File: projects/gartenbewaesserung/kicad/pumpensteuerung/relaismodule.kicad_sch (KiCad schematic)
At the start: 5 parts, among them J1 Screw_Terminal_01x03, K2 SANYOU_SRD_Form_C, Q1 S8050

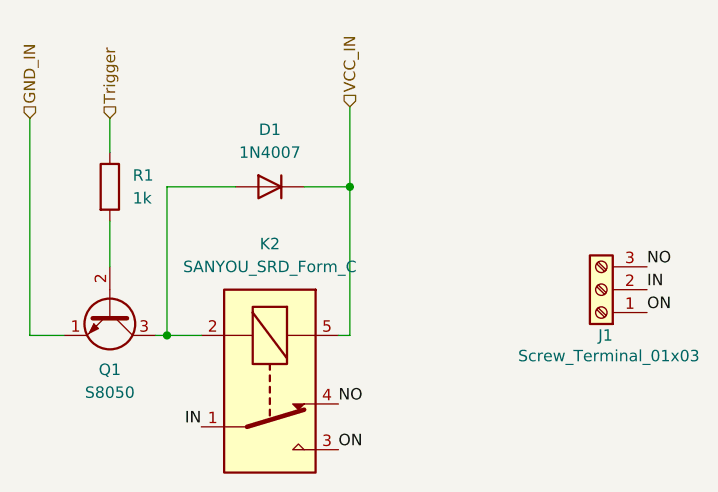
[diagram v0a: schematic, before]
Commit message: [gartenbewaesserung(pcb)] change resistor to 220 Ohm
1k was a little bit too much, for 3.3V.
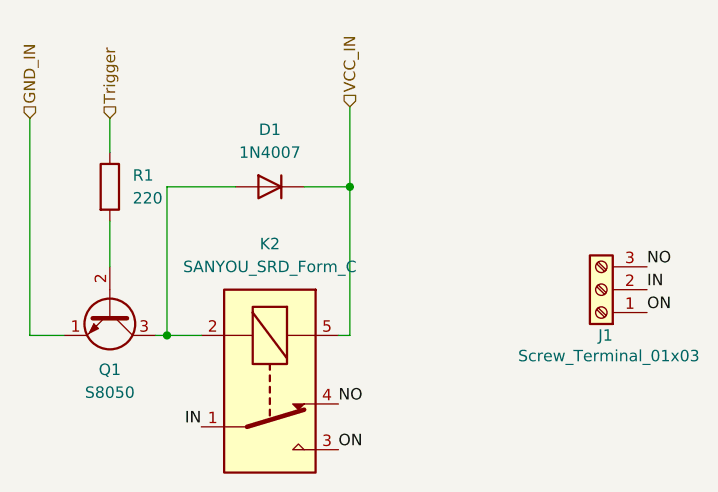
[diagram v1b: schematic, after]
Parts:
- R1: value 1k -> 220; footprint Resistor_THT:R_Axial_DIN0204_L3.6mm_D1.6mm_P7.62mm_Horizontal -> Resistor_THT:R_Axial_DIN0207_L6.3mm_D2.5mm_P7.62mm_Horizontal
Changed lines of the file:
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@@
 			)
 		)
-		(property "Value" "1k"
+		(property "Value" "220"
 			(at 30.48 31.7499 0)
 			(effects
@@
 			)
 		)
-		(property "Footprint" "Resistor_THT:R_Axial_DIN0204_L3.6mm_D1.6mm_P7.62mm_Horizontal"
+		(property "Footprint" "Resistor_THT:R_Axial_DIN0207_L6.3mm_D2.5mm_P7.62mm_Horizontal"
 			(at 26.162 30.48 90)
 			(effects

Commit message: [gartenbewasserung(pcb)] replace Q8050 with a 2N3904
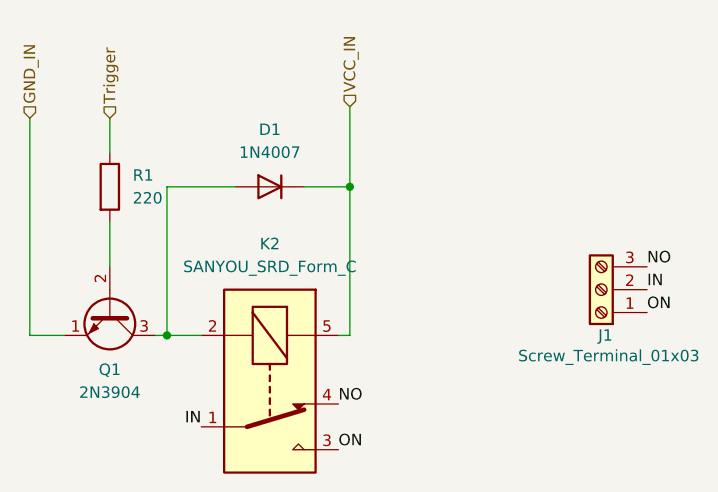
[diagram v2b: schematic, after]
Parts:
- removed Q1: S8050, Package_TO_SOT_THT:TO-92_Inline, symbol Transistor_BJT:S8050
- added Q1: 2N3904, Package_TO_SOT_THT:TO-92_Inline, symbol Transistor_BJT:2N3904
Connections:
- net GND_IN: now also Q1.1 (E)
- net at R1.2: now also Q1.2 (B)
- net at D1.2 (A), K2.2: now also Q1.3 (C)
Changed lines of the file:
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@@
-	)
-	(symbol
-		(lib_id "Transistor_BJT:S8050")
-		(at 27.94 44.45 270)
-		(unit 1)
-		(exclude_from_sim no)
-		(in_bom yes)
-		(on_board yes)
-		(dnp no)
-		(fields_autoplaced yes)
-		(property "Reference" "Q1"
-			(at 27.94 50.8 90)
-			(effects
-				(font
-					(size 1.27 1.27)
-				)
-			)
-		)
-		(property "Value" "S8050"
-			(at 27.94 53.34 90)
-			(effects
-				(font
-					(size 1.27 1.27)
-				)
-			)
-		)
-		(property "Footprint" "Package_TO_SOT_THT:TO-92_Inline"
-			(at 26.035 49.53 0)
-			(effects
-				(font
-					(size 1.27 1.27)
-					(italic yes)
-				)
-				(justify left)
-				(hide yes)
-			)
-		)
-		(property "Datasheet" "http://www.unisonic.com.tw/datasheet/S8050.pdf"
-			(at 27.94 44.45 0)
-			(effects
-				(font
-					(size 1.27 1.27)
-				)
-				(justify left)
-				(hide yes)
-			)
-		)
-		(property "Description" "0.7A Ic, 20V Vce, Low Voltage High Current NPN Transistor, TO-92"
-			(at 27.94 44.45 0)
-			(effects
-				(font
-					(size 1.27 1.27)
-				)
-				(hide yes)
-			)
-		)
-		(pin "3"
-		)
-		(pin "1"
-		)
-		(pin "2"
-		)
-		(instances
-			(project "gartenbewaesserung"
-				(path "/21a07dfa-371b-4773-840e-44a8dfeac208/016a9bfd-fffd-4284-b312-eaf12770d68d"
-					(reference "Q1")
-					(unit 1)
-				)
-				(path "/21a07dfa-371b-4773-840e-44a8dfeac208/63189825-b5eb-44b8-a12d-37b83fa5c151"
-					(reference "Q3")
-					(unit 1)
-				)
-				(path "/21a07dfa-371b-4773-840e-44a8dfeac208/d92ddb11-359c-4ecb-a782-88a2addaf04a"
-					(reference "Q2")
-					(unit 1)
-				)
-			)
-		)
 	)
 	(symbol
@@
 					(unit 1)
 				)
+			)
+		)
+	)
+	(symbol
+		(lib_id "Transistor_BJT:2N3904")
+		(at 27.94 44.45 270)
+		(unit 1)
+		(exclude_from_sim no)
+		(in_bom yes)
+		(on_board yes)
+		(dnp no)
+		(fields_autoplaced yes)
+		(property "Reference" "Q1"
+			(at 27.94 50.8 90)
+			(effects
+				(font
+					(size 1.27 1.27)
+				)
+			)
+		)
+		(property "Value" "2N3904"
+			(at 27.94 53.34 90)
+			(effects
+				(font
+					(size 1.27 1.27)
+				)
+			)
+		)
+		(property "Footprint" "Package_TO_SOT_THT:TO-92_Inline"
+			(at 26.035 49.53 0)
+			(effects
+				(font
+					(size 1.27 1.27)
+					(italic yes)
+				)
+				(justify left)
+				(hide yes)
+			)
+		)
+		(property "Datasheet" "https://www.onsemi.com/pub/Collateral/2N3903-D.PDF"
+			(at 27.94 44.45 0)
+			(effects
+				(font
+					(size 1.27 1.27)
+				)
+				(justify left)
+				(hide yes)
+			)
+		)
+		(property "Description" "0.2A Ic, 40V Vce, Small Signal NPN Transistor, TO-92"
+			(at 27.94 44.45 0)
+			(effects
+				(font
+					(size 1.27 1.27)
+				)
+				(hide yes)
+			)
+		)
+		(pin "2"
+		)
+		(pin "1"
+		)
+		(pin "3"
+		)
+		(instances
+			(project ""
+				(path "/21a07dfa-371b-4773-840e-44a8dfeac208/016a9bfd-fffd-4284-b312-eaf12770d68d"
+					(reference "Q1")
+					(unit 1)
+				)
+				(path "/21a07dfa-371b-4773-840e-44a8dfeac208/63189825-b5eb-44b8-a12d-37b83fa5c151"
+					(reference "Q3")
+					(unit 1)
+				)
+				(path "/21a07dfa-371b-4773-840e-44a8dfeac208/d92ddb11-359c-4ecb-a782-88a2addaf04a"
+					(reference "Q2")
+					(unit 1)
+				)

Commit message: [gartenbewaesserung(pcb)] add MPN to easier pcb ordering
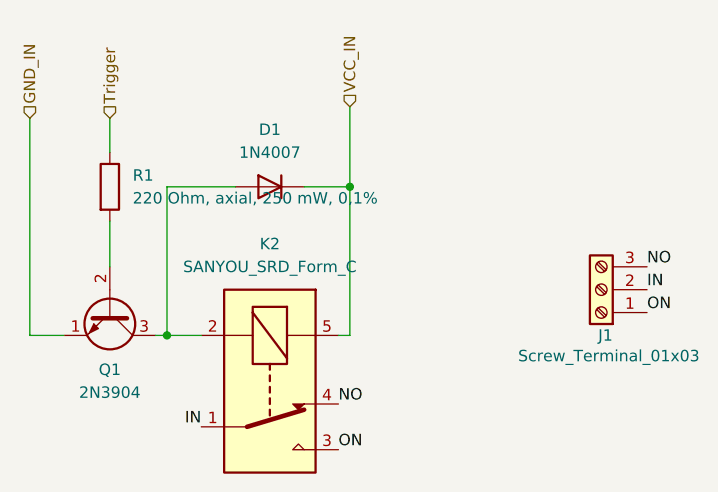
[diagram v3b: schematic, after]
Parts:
- D1: MPN (none) -> 1N4007
- J1: MPN (none) -> 1729131
- K2: MPN (none) -> HF3FA/005-ZTF
- Q1: MPN (none) -> 2N3904
- R1: value 220 -> 220 Ohm, axial, 250 mW, 0,1%; MPN (none) -> RC55Y-220RBI
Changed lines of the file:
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@@
 			)
 		)
-		(property "Value" "220"
+		(property "Value" "220 Ohm, axial, 250 mW, 0,1%"
 			(at 30.48 31.7499 0)
 			(effects
@@
 		)
 		(property "Description" "Resistor"
+			(at 27.94 30.48 0)
+			(effects
+				(font
+					(size 1.27 1.27)
+				)
+				(hide yes)
+			)
+		)
+		(property "MPN" " RC55Y-220RBI"
 			(at 27.94 30.48 0)
 			(effects
@@
 			)
 		)
+		(property "MPN" "1N4007"
+			(at 45.72 30.48 0)
+			(effects
+				(font
+					(size 1.27 1.27)
+				)
+				(hide yes)
+			)
+		)
 		(pin "2"
 		)
@@
 		)
 		(property "Description" "Generic screw terminal, single row, 01x03, script generated (kicad-library-utils/schlib/autogen/connector/)"
+			(at 82.55 41.91 0)
+			(effects
+				(font
+					(size 1.27 1.27)
+				)
+				(hide yes)
+			)
+		)
+		(property "MPN" "1729131"
 			(at 82.55 41.91 0)
 			(effects
@@
 			)
 		)
+		(property "MPN" "2N3904"
+			(at 27.94 44.45 90)
+			(effects
+				(font
+					(size 1.27 1.27)
+				)
+				(hide yes)
+			)
+		)
 		(pin "2"
 		)
@@
 			(effects
 				(font
+					(size 1.27 1.27)
+				)
+				(hide yes)
+			)
+		)
+		(property "MPN" "HF3FA/005-ZTF"
+			(at 45.72 52.07 90)
+			(effects
+				(font

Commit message: [gartenbewaesserung(pcb)] replace resistor with one from vishay
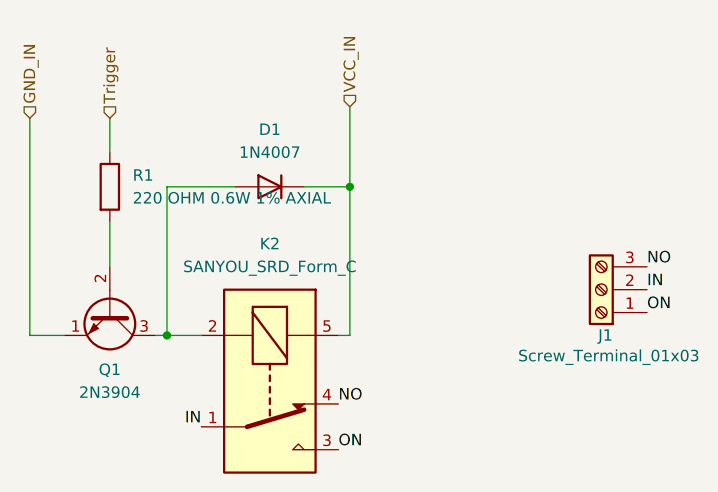
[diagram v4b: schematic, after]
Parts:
- R1: value 220 Ohm, axial, 250 mW, 0,1% -> 220 OHM 0.6W 1% AXIAL; MPN RC55Y-220RBI -> MBB02070C2200FCT00
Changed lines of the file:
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@@
 			)
 		)
-		(property "Value" "220 Ohm, axial, 250 mW, 0,1%"
+		(property "Value" "220 OHM 0.6W 1% AXIAL"
 			(at 30.48 31.7499 0)
 			(effects
@@
 			)
 		)
-		(property "Datasheet" "~"
+		(property "Datasheet" "https://www.vishay.com/docs/28766/mbxsma.pdf"
 			(at 27.94 30.48 0)
 			(effects
@@
 			)
 		)
-		(property "MPN" " RC55Y-220RBI"
+		(property "MPN" "MBB02070C2200FCT00"
 			(at 27.94 30.48 0)
 			(effects
